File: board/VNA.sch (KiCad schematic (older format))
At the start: 75 parts, among them J1 Conn_02x07_Odd_Even, J10 Conn_01x01, J11 Conn_01x01, J12 Conn_01x01, J13 Barrel_Jack, J15 Conn_02x05_Odd_Even, J17 Conn_01x04, J18 Conn_01x01, J19 Conn_01x01, J2 Conn_Coaxial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

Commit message: Added JST 2.54 power and USB-B connecotrs
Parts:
- added J14: Conn_01x02, Connectors_Molex:Molex_KK-6410-02_02x2.54mm_Straight, symbol Conn_01x02
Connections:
- net GND: now also J14.1 (Pin_1)
- net at C47.1, J13.1, J22.2 (Pin_2)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: now also J14.2 (Pin_2)
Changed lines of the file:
@@
 $EndComp
 $Comp
-L GND #PWR16
+L GND #PWR15
 U 1 1 5BB182B4
 P 2600 7450
-F 0 "#PWR16" H 2600 7200 50  0001 C CNN
+F 0 "#PWR15" H 2600 7200 50  0001 C CNN
 F 1 "GND" H 2600 7300 50  0000 C CNN
 F 2 "" H 2600 7450 50  0001 C CNN
@@
 $EndComp
 $Comp
-L GND #PWR21
+L GND #PWR20
 U 1 1 5BB1B358
 P 3000 7450
-F 0 "#PWR21" H 3000 7200 50  0001 C CNN
+F 0 "#PWR20" H 3000 7200 50  0001 C CNN
 F 1 "GND" H 3000 7300 50  0000 C CNN
 F 2 "" H 3000 7450 50  0001 C CNN
@@
 $EndComp
 $Comp
-L GND #PWR18
+L GND #PWR17
 U 1 1 5BB20C8C
 P 2900 2900
-F 0 "#PWR18" H 2900 2650 50  0001 C CNN
+F 0 "#PWR17" H 2900 2650 50  0001 C CNN
 F 1 "GND" H 2900 2750 50  0000 C CNN
 F 2 "" H 2900 2900 50  0001 C CNN
@@
 $EndComp
 $Comp
-L GND #PWR22
+L GND #PWR21
 U 1 1 5BB222C0
 P 3400 2900
-F 0 "#PWR22" H 3400 2650 50  0001 C CNN
+F 0 "#PWR21" H 3400 2650 50  0001 C CNN
 F 1 "GND" H 3400 2750 50  0000 C CNN
 F 2 "" H 3400 2900 50  0001 C CNN
@@
 DEMODCUR2
 $Comp
-L GND #PWR19
+L GND #PWR18
 U 1 1 5BB4A165
 P 2950 5400
-F 0 "#PWR19" H 2950 5150 50  0001 C CNN
+F 0 "#PWR18" H 2950 5150 50  0001 C CNN
 F 1 "GND" H 2950 5250 50  0000 C CNN
 F 2 "" H 2950 5400 50  0001 C CNN
@@
 $EndComp
 $Comp
-L +5V #PWR48
+L +5V #PWR47
 U 1 1 5BB3F764
 P 10700 5200
-F 0 "#PWR48" H 10700 5050 50  0001 C CNN
+F 0 "#PWR47" H 10700 5050 50  0001 C CNN
 F 1 "+5V" H 10700 5340 50  0000 C CNN
 F 2 "" H 10700 5200 50  0001 C CNN
@@
 $EndComp
 $Comp
-L GND #PWR49
+L GND #PWR48
 U 1 1 5BB3F96D
 P 10700 5550
-F 0 "#PWR49" H 10700 5300 50  0001 C CNN
+F 0 "#PWR48" H 10700 5300 50  0001 C CNN
 F 1 "GND" H 10700 5400 50  0000 C CNN
 F 2 "" H 10700 5550 50  0001 C CNN
@@
 $EndComp
 $Comp
-L GND #PWR15
-U 1 1 5BB34A68
-P 2500 3800
-F 0 "#PWR15" H 2500 3550 50  0001 C CNN
-F 1 "GND" H 2500 3650 50  0000 C CNN
-F 2 "" H 2500 3800 50  0001 C CNN
-F 3 "" H 2500 3800 50  0001 C CNN
-	1    2500 3800
-	1    0    0    -1
-$EndComp
-$Comp
-L +5V #PWR27
+L +5V #PWR26
 U 1 1 5BB34D5D
 P 3800 3550
-F 0 "#PWR27" H 3800 3400 50  0001 C CNN
+F 0 "#PWR26" H 3800 3400 50  0001 C CNN
 F 1 "+5V" H 3800 3690 50  0000 C CNN
 F 2 "" H 3800 3550 50  0001 C CNN
@@
 $EndComp
 $Comp
-L GND #PWR23
+L GND #PWR22
 U 1 1 5BB368A3
 P 3400 7450
-F 0 "#PWR23" H 3400 7200 50  0001 C CNN
+F 0 "#PWR22" H 3400 7200 50  0001 C CNN
 F 1 "GND" H 3400 7300 50  0000 C CNN
 F 2 "" H 3400 7450 50  0001 C CNN
@@
 $EndComp
 $Comp
-L GND #PWR43
+L GND #PWR49
 U 1 1 5BB37FFB
 P 11200 4800
-F 0 "#PWR43" H 11200 4550 50  0001 C CNN
+F 0 "#PWR49" H 11200 4550 50  0001 C CNN
 F 1 "GND" H 11200 4650 50  0000 C CNN
 F 2 "" H 11200 4800 50  0001 C CNN
@@
 $EndComp
 $Comp
-L GND #PWR17
+L GND #PWR16
 U 1 1 5BB39581
 P 2700 4200
-F 0 "#PWR17" H 2700 3950 50  0001 C CNN
+F 0 "#PWR16" H 2700 3950 50  0001 C CNN
 F 1 "GND" H 2700 4050 50  0000 C CNN
 F 2 "" H 2700 4200 50  0001 C CNN
@@
 $EndComp
 $Comp
-L GND #PWR24
+L GND #PWR23
 U 1 1 5BB39BBE
 P 3500 4050
-F 0 "#PWR24" H 3500 3800 50  0001 C CNN
+F 0 "#PWR23" H 3500 3800 50  0001 C CNN
 F 1 "GND" H 3500 3900 50  0000 C CNN
 F 2 "" H 3500 4050 50  0001 C CNN
@@
 $EndComp
 $Comp
-L GND #PWR20
+L GND #PWR19
 U 1 1 5BD7CAFC
 P 3000 4100
-F 0 "#PWR20" H 3000 3850 50  0001 C CNN
+F 0 "#PWR19" H 3000 3850 50  0001 C CNN
 F 1 "GND" H 3000 3950 50  0000 C CNN
 F 2 "" H 3000 4100 50  0001 C CNN
@@
 PB10
 $Comp
-L +3V3 #PWR47
+L +3V3 #PWR46
 U 1 1 5BB22189
 P 10550 1600
-F 0 "#PWR47" H 10550 1450 50  0001 C CNN
+F 0 "#PWR46" H 10550 1450 50  0001 C CNN
 F 1 "+3V3" H 10550 1740 50  0000 C CNN
 F 2 "" H 10550 1600 50  0001 C CNN
@@
 $EndComp
 $Comp
-L GND #PWR29
+L GND #PWR28
 U 1 1 5BFEB64E
 P 4050 5600
-F 0 "#PWR29" H 4050 5350 50  0001 C CNN
+F 0 "#PWR28" H 4050 5350 50  0001 C CNN
 F 1 "GND" H 4050 5450 50  0000 C CNN
 F 2 "" H 4050 5600 50  0001 C CNN
@@
 $EndComp
 $Comp
-L GND #PWR31
+L GND #PWR30
 U 1 1 5BFEBC91
 P 4750 5600
-F 0 "#PWR31" H 4750 5350 50  0001 C CNN
+F 0 "#PWR30" H 4750 5350 50  0001 C CNN
 F 1 "GND" H 4750 5450 50  0000 C CNN
 F 2 "" H 4750 5600 50  0001 C CNN
@@
 $EndComp
 $Comp
-L GND #PWR28
+L GND #PWR27
 U 1 1 5BFED2D3
 P 3800 4200
-F 0 "#PWR28" H 3800 3950 50  0001 C CNN
+F 0 "#PWR27" H 3800 3950 50  0001 C CNN
 F 1 "GND" H 3800 4050 50  0000 C CNN
 F 2 "" H 3800 4200 50  0001 C CNN
@@
 $EndComp
 $Comp
-L GND #PWR26
+L GND #PWR25
 U 1 1 5C012A71
 P 3750 7450
-F 0 "#PWR26" H 3750 7200 50  0001 C CNN
+F 0 "#PWR25" H 3750 7200 50  0001 C CNN
 F 1 "GND" H 3750 7300 50  0000 C CNN
 F 2 "" H 3750 7450 50  0001 C CNN
@@
 $EndComp
 $Comp
-L GND #PWR46
+L GND #PWR31
 U 1 1 5C1BDCBD
 P 5200 5900
-F 0 "#PWR46" H 5200 5650 50  0001 C CNN
+F 0 "#PWR31" H 5200 5650 50  0001 C CNN
 F 1 "GND" H 5200 5750 50  0000 C CNN
 F 2 "" H 5200 5900 50  0001 C CNN
@@
 $EndComp
 $Comp
-L GND #PWR25
+L GND #PWR24
 U 1 1 5D91CAF8
 P 3500 6400
-F 0 "#PWR25" H 3500 6150 50  0001 C CNN
+F 0 "#PWR24" H 3500 6150 50  0001 C CNN
 F 1 "GND" H 3500 6250 50  0000 C CNN
 F 2 "" H 3500 6400 50  0001 C CNN
@@
 $EndComp
 $Comp
-L GND #PWR30
+L GND #PWR29
 U 1 1 5D91CBC7
 P 4500 6400
-F 0 "#PWR30" H 4500 6150 50  0001 C CNN
+F 0 "#PWR29" H 4500 6150 50  0001 C CNN
 F 1 "GND" H 4500 6250 50  0000 C CNN
 F 2 "" H 4500 6400 50  0001 C CNN
@@
 $EndComp
 $Comp
-L +5V #PWR?
+L +5V #PWR43
 U 1 1 5DB1B8AD
 P 10150 4550
-F 0 "#PWR?" H 10150 4400 50  0001 C CNN
+F 0 "#PWR43" H 10150 4400 50  0001 C CNN
 F 1 "+5V" H 10150 4690 50  0000 C CNN
 F 2 "" H 10150 4550 50  0001 C CNN
@@
 Connection ~ 2450 3650
 Wire Wire Line
-	2450 3150 2450 3650
+	2450 3150 2450 4050
 Wire Wire Line
 	2350 3150 2450 3150
@@
 	2250 3650 2700 3650
 Wire Wire Line
-	2500 3750 2500 3800
-Wire Wire Line
-	2250 3750 2500 3750
+	2500 3750 2500 4150
+Wire Wire Line
+	2250 3750 2550 3750
 Wire Wire Line
 	9200 5400 10800 5400
@@
 Wire Wire Line
 	10850 4550 10150 4550
+Wire Wire Line
+	2550 3750 2550 4150
+Wire Wire Line
+	2550 4150 2700 4150
+Connection ~ 2700 4150
+Connection ~ 2500 3750
+$Comp
+L Conn_01x02 J14
+U 1 1 5DCAEE79
+P 2050 4150
+F 0 "J14" H 2050 4250 50  0000 C CNN
+F 1 "Conn_01x02" H 2050 3950 50  0000 C CNN
+F 2 "Connectors_Molex:Molex_KK-6410-02_02x2.54mm_Straight" H 2050 4150 50  0001 C CNN
+F 3 "" H 2050 4150 50  0001 C CNN
+	1    2050 4150
+	-1   0    0    1
+$EndComp
+Wire Wire Line
+	2500 4150 2250 4150
+Wire Wire Line
+	2450 4050 2250 4050
 $EndSCHEMATC

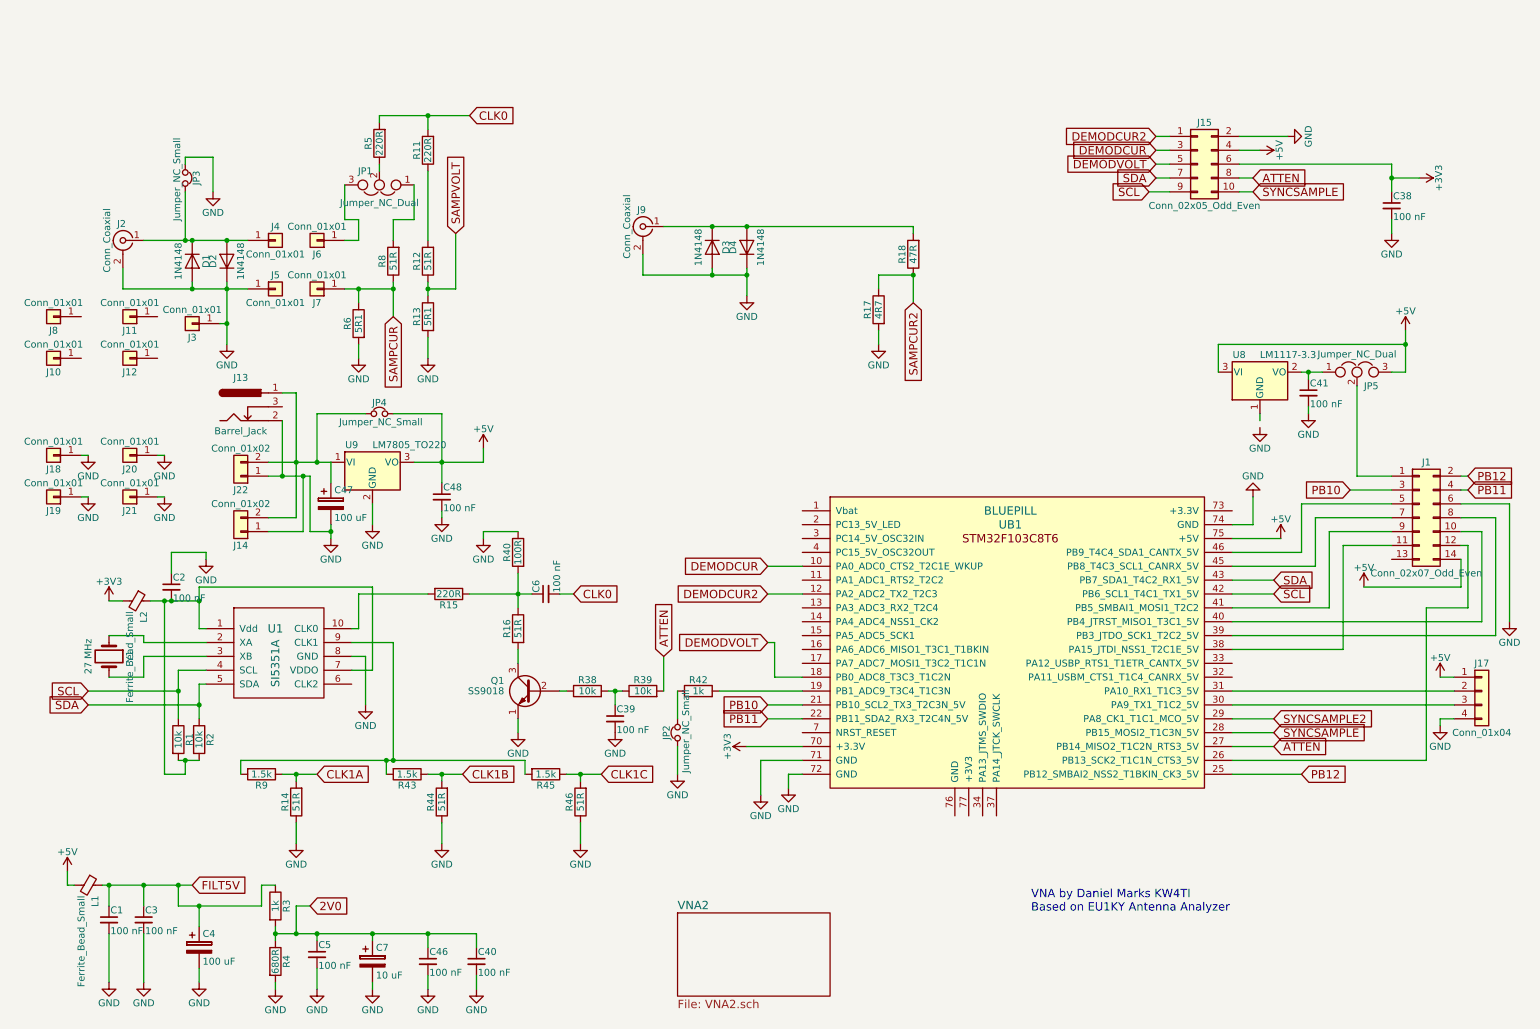
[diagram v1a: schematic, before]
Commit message: Changes to finalize two SI5351A solution
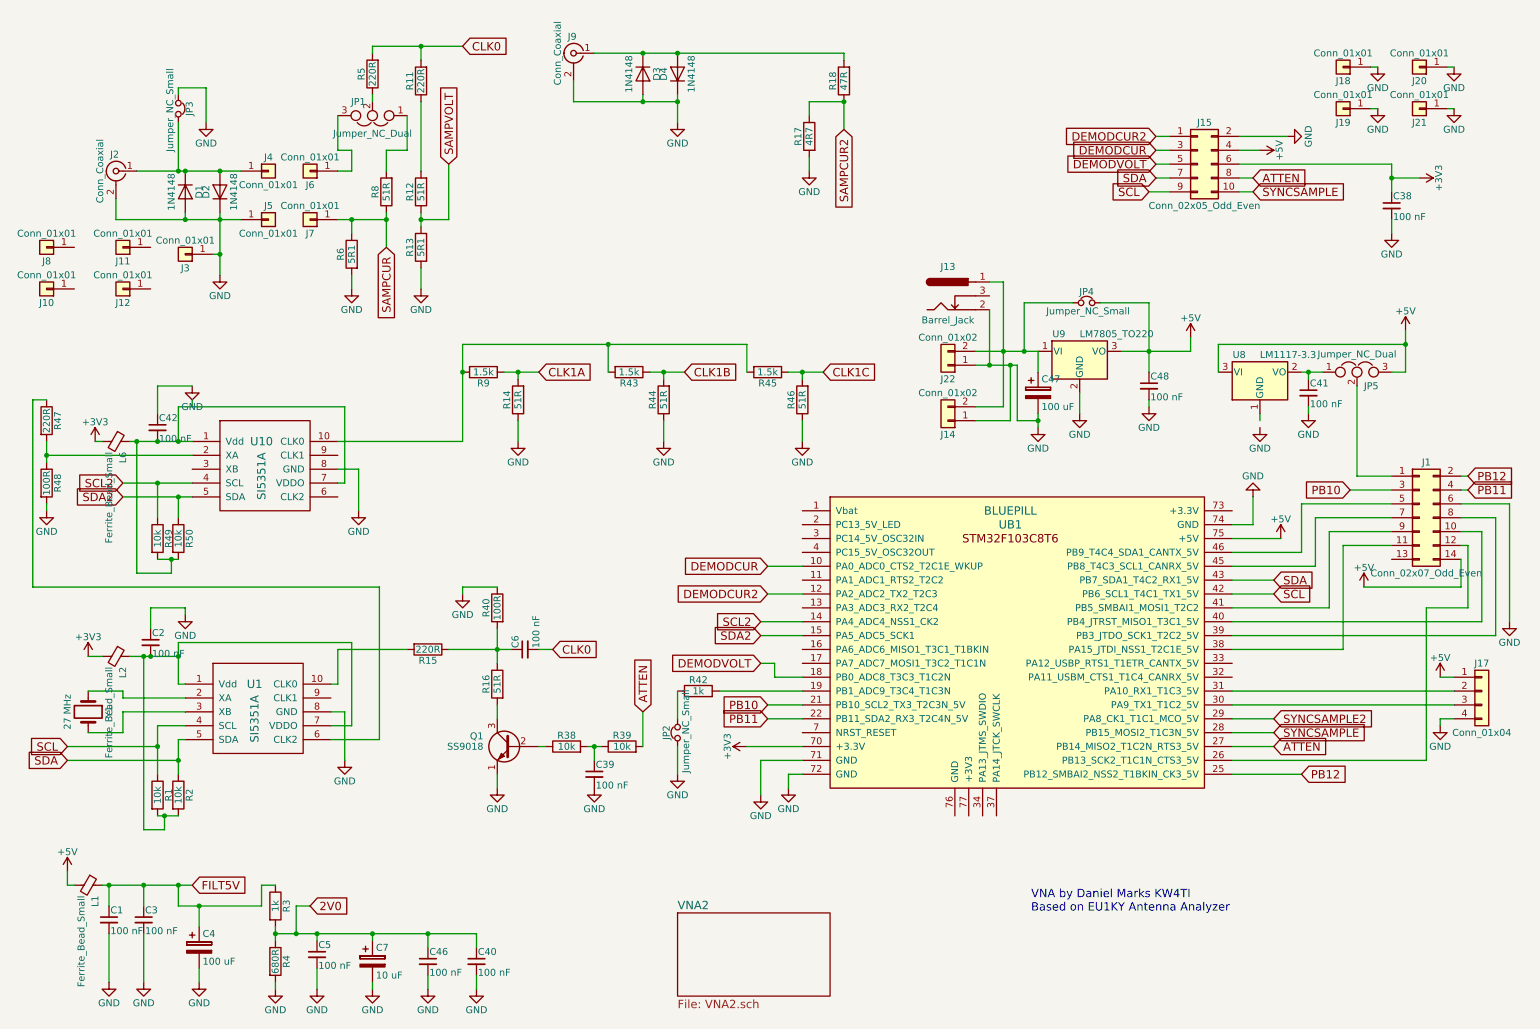
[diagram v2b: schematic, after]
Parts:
- added C42: 100 nF, Capacitors_THT:C_Disc_D5.0mm_W2.5mm_P2.50mm, symbol C_Small
- added L6: Ferrite_Bead_Small, Inductors_THT:L_Axial_L5.3mm_D2.2mm_P7.62mm_Horizontal_Vishay_IM-1, symbol Ferrite_Bead_Small
- added R47: 220R, Resistors_THT:R_Axial_DIN0207_L6.3mm_D2.5mm_P7.62mm_Horizontal, symbol R
- added R48: 100R, Resistors_THT:R_Axial_DIN0207_L6.3mm_D2.5mm_P7.62mm_Horizontal, symbol R
- added R49, R50: 10k, Resistors_THT:R_Axial_DIN0207_L6.3mm_D2.5mm_P7.62mm_Horizontal, symbol R
- added U10: SI5351A, Housings_SSOP:MSOP-10_3x3mm_Pitch0.5mm, symbol SI5351A
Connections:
- net +3V3: now also L6.2
- net GND: now also C42.1, R48.2, U10.8 (GND)
- net SCL2: now reaches UB1.14 (PA4_ADC4_NSS1_CK2)
- net SCL2: now also R49.1, U10.4 (SCL)
- net SDA2: now reaches UB1.15 (PA5_ADC5_SCK1)
- net SDA2: now also R50.1, U10.5 (SDA)
- net at U1.6 (CLK2): now also R47.1
- net at R43.2, R45.2, R9.2: now also U10.10 (CLK0); no longer U1.9 (CLK1)
- new net: C42.2, L6.1, R49.2, R50.2, U10.1 (Vdd), U10.7 (VDDO)
- new net: R47.2, R48.1, U10.2 (XA)
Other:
- moved on the sheet: C2, C39, C47, C48, C6, D1, D2, D3, D4, J10, J11, J12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

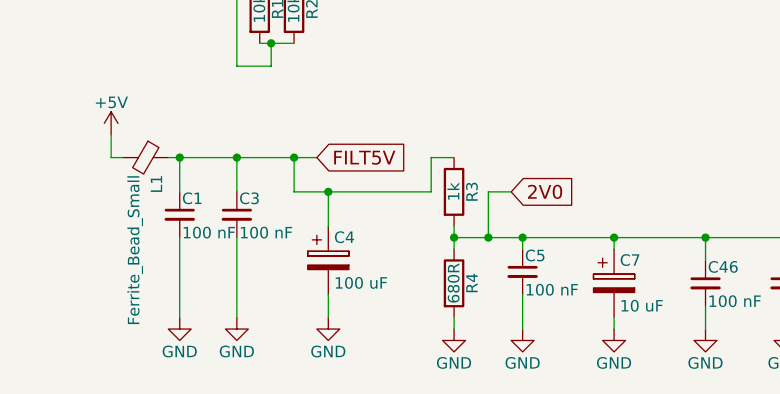
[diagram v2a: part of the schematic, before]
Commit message: Changed pullup resistors to 10k for less supply noise
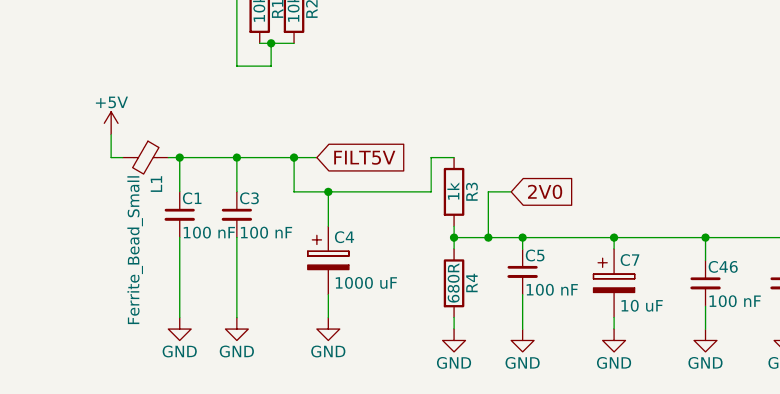
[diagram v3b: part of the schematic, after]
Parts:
- C4: value 100 uF -> 1000 uF
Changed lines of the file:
@@
 P 1750 7150
 F 0 "C4" H 1775 7250 50  0000 L CNN
-F 1 "100 uF" H 1775 7050 50  0000 L CNN
+F 1 "1000 uF" H 1775 7050 50  0000 L CNN
 F 2 "Capacitors_THT:CP_Radial_D5.0mm_P2.50mm" H 1788 7000 50  0001 C CNN
 F 3 "" H 1750 7150 50  0001 C CNN

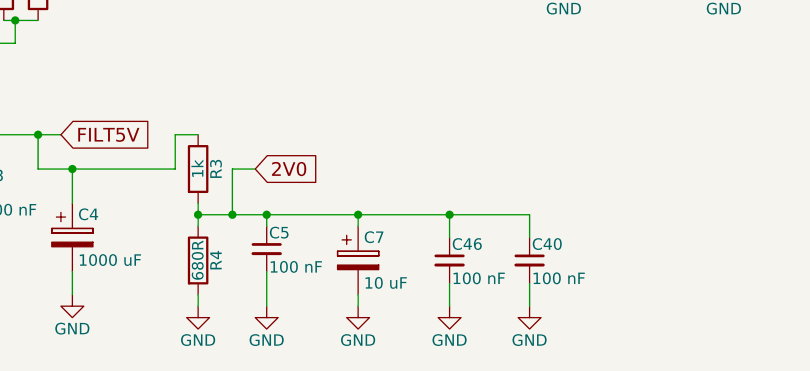
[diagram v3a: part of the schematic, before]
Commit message: Updated software to add cursor for smith chart, also changed edge of triggering
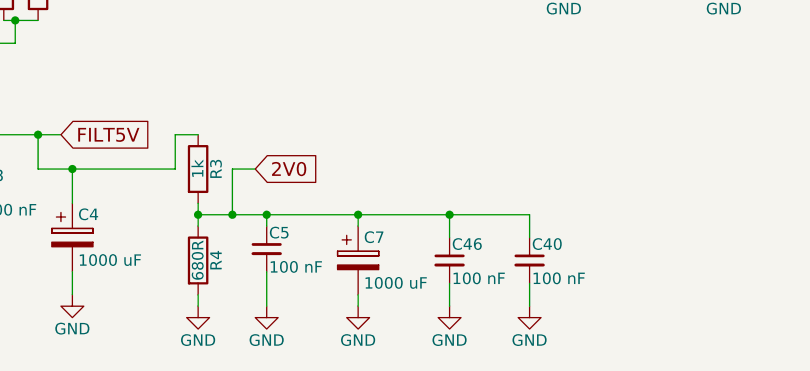
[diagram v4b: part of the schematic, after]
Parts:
- C4: footprint Capacitors_THT:CP_Radial_D5.0mm_P2.50mm -> Capacitors_THT:CP_Radial_D10.0mm_P5.00mm
- C7: value 10 uF -> 1000 uF; footprint Capacitors_THT:CP_Radial_D5.0mm_P2.50mm -> Capacitors_THT:CP_Radial_D10.0mm_P5.00mm
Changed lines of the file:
@@
 F 0 "C4" H 1775 7250 50  0000 L CNN
 F 1 "1000 uF" H 1775 7050 50  0000 L CNN
-F 2 "Capacitors_THT:CP_Radial_D5.0mm_P2.50mm" H 1788 7000 50  0001 C CNN
+F 2 "Capacitors_THT:CP_Radial_D10.0mm_P5.00mm" H 1788 7000 50  0001 C CNN
 F 3 "" H 1750 7150 50  0001 C CNN
 	1    1750 7150
@@
 P 3000 7250
 F 0 "C7" H 3025 7350 50  0000 L CNN
-F 1 "10 uF" H 3025 7150 50  0000 L CNN
-F 2 "Capacitors_THT:CP_Radial_D5.0mm_P2.50mm" H 3038 7100 50  0001 C CNN
+F 1 "1000 uF" H 3025 7150 50  0000 L CNN
+F 2 "Capacitors_THT:CP_Radial_D10.0mm_P5.00mm" H 3038 7100 50  0001 C CNN
 F 3 "" H 3000 7250 50  0001 C CNN
 	1    3000 7250
